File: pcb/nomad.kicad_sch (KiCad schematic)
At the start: 36 parts, among them J1 USB_C_Receptacle_USB2.0_16P, J2 Conn_Coaxial, SW1 SW_Push, SW2 SW_Push, SW3 SW_Push, SW4 SW_Push, SW5 SW_Push, SW6 SW_Push, SW7 SW_Push, U1 ESP32-S3-WROOM-1, U2 PCF8574T, U3 BME280, U4 NEO-M8M, U5 CH343G, U7 AMS1117-3.3

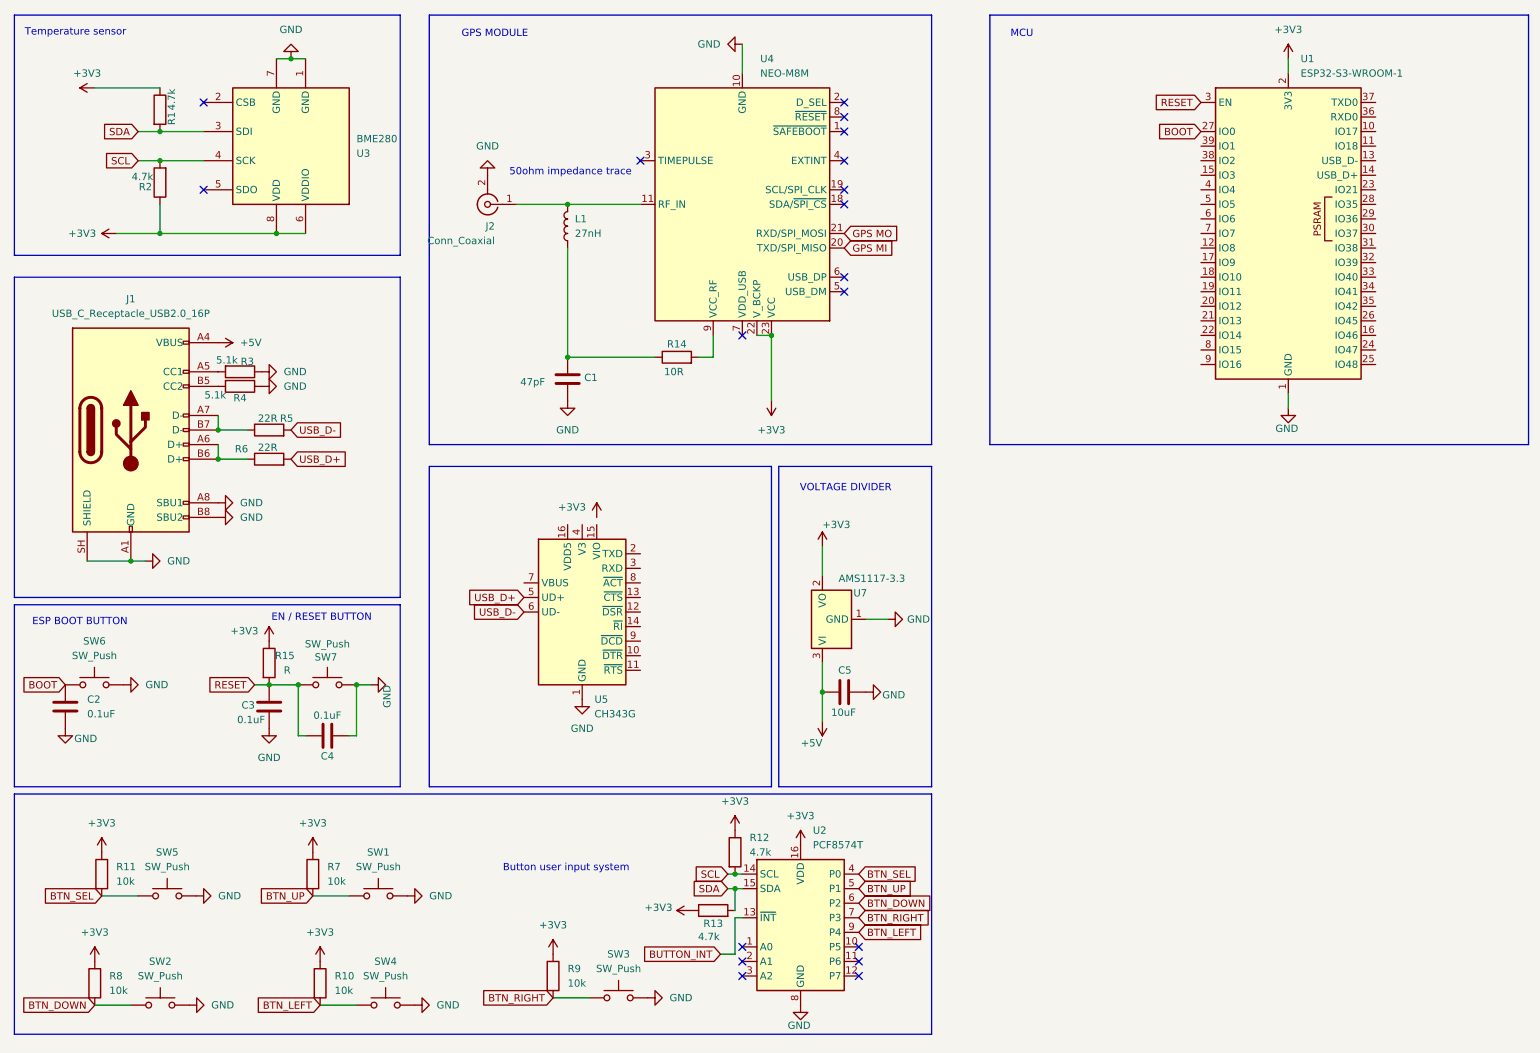
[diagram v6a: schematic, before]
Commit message: Separating modules schematic with system schematic
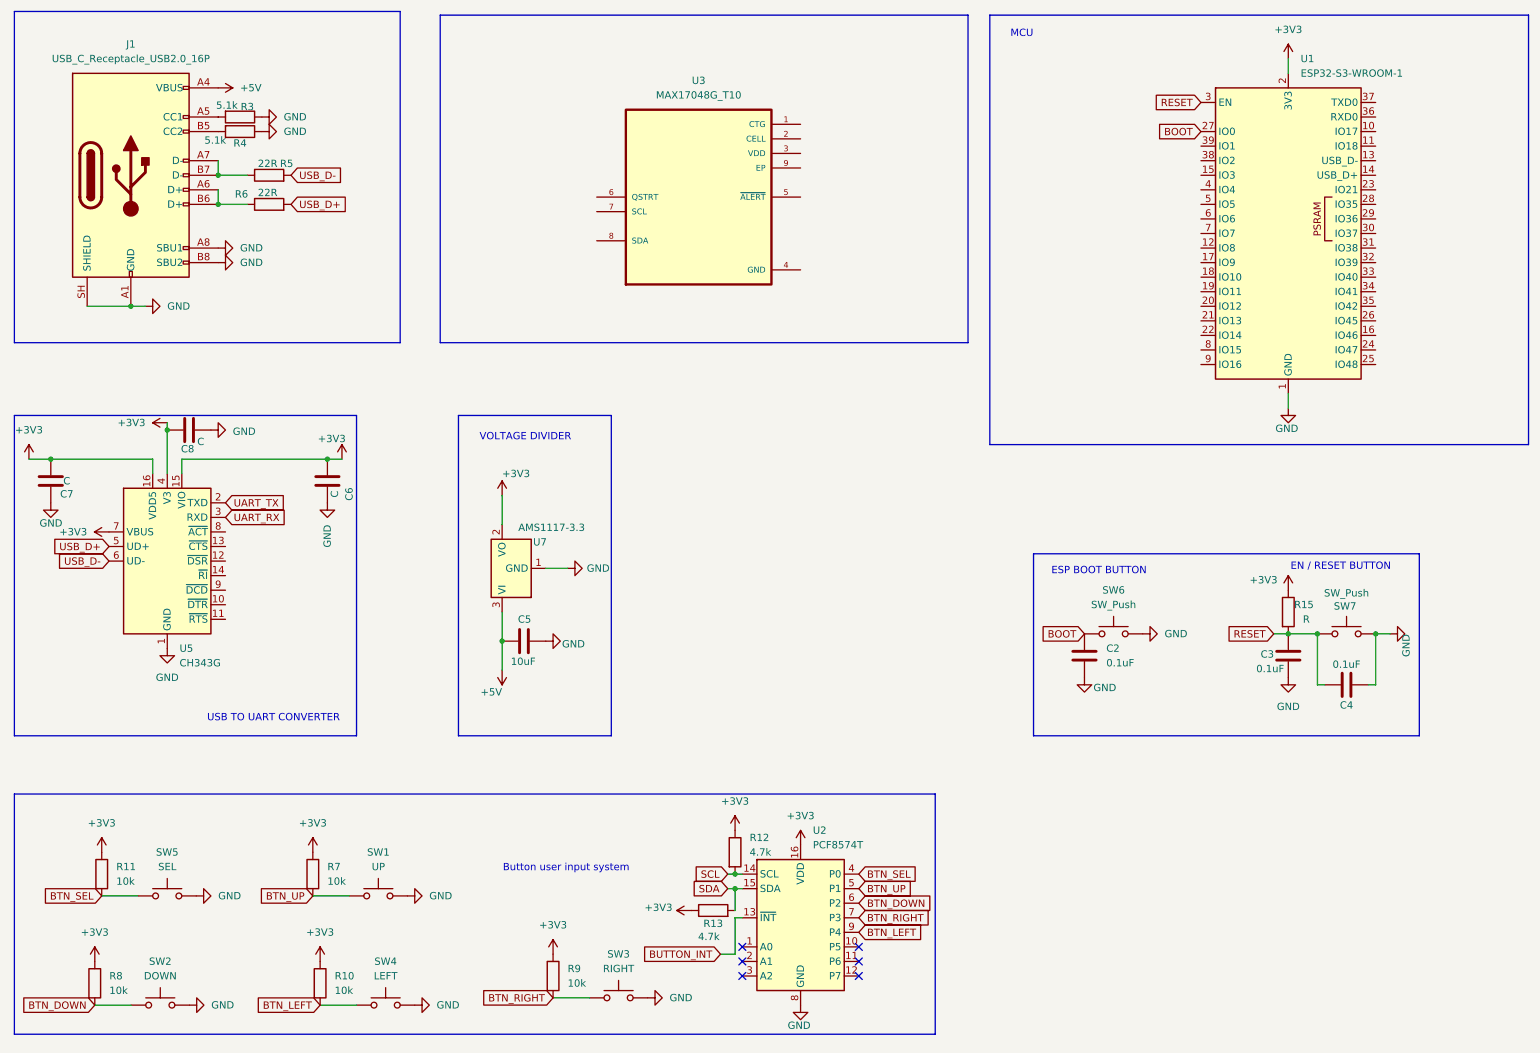
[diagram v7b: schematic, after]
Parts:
- removed C1: 47pF, Capacitor_SMD:C_0805_2012Metric, symbol Device:C
- removed J2: Conn_Coaxial, symbol Connector:Conn_Coaxial
- removed L1: 27nH, symbol Device:L
- removed R1, R2: 4.7k, symbol Device:R
- removed R14: 10R, symbol Device:R
- removed U3: BME280, Package_LGA:Bosch_LGA-8_2.5x2.5mm_P0.65mm_ClockwisePinNumbering, symbol Sensor:BME280
- removed U4: NEO-M8M, RF_GPS:ublox_NEO, symbol RF_GPS:NEO-M8M
- added C6, C7, C8: C, symbol Device:C
- added U3: MAX17048G_T10, MAX17048G_T10:SON50P200X200X80-9N, symbol MAX17048G_T10:MAX17048G_T10
- R10, R11, R12, R13, R15, R3, R4, R5, R6, R7, R8, R9: footprint (none) -> Resistor_SMD:R_0805_2012Metric
- SW1: value SW_Push -> UP; footprint (none) -> Button_Switch_THT:SW_PUSH_6mm
- SW2: value SW_Push -> DOWN; footprint (none) -> Button_Switch_THT:SW_PUSH_6mm
- SW3: value SW_Push -> RIGHT; footprint (none) -> Button_Switch_THT:SW_PUSH_6mm
- SW4: value SW_Push -> LEFT; footprint (none) -> Button_Switch_THT:SW_PUSH_6mm
- SW5: value SW_Push -> SEL; footprint (none) -> Button_Switch_THT:SW_PUSH_6mm
- SW6, SW7: footprint (none) -> Button_Switch_SMD:SW_SPST_SKQG_WithStem
- U1: footprint RF_Module:ESP32-S3-WROOM-1 -> RF_Module:ESP32-S3-WROOM-1U
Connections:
- net +3V3: now also U5.15 (VIO), U5.16 (VDD5), U5.4 (V3), U5.7 (VBUS), C6.1, C7.2, C8.1
- net GND: now also C6.2, C7.1, C8.2
- net UART_TX: now reaches U5.2 (TXD)
- net UART_RX: now reaches U5.3 (RXD)
- no-connect marks 18 -> 6
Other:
- note added: "USB TO UART CONVERTER"
- note removed: "50ohm impedance trace"
- note removed: "GPS MODULE"
- note removed: "Temperature sensor"
- moved on the sheet: C2, C3, C4, C5, J1, R15, R3, R4, R5, R6, SW6, SW7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

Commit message: Updating schematic & pcb & BOM
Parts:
- added C1, C10, C11: C, symbol Device:C
- C5, C6, C7, C8: footprint (none) -> Capacitor_SMD:C_0805_2012Metric
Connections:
- net +3V3: now also C1.1, C10.1, C11.1
- net GND: now also U3.4 (GND), C1.2, C10.2, C11.2
- net SCL: now also U3.7 (SCL)
- net SDA: now also U3.8 (SDA)
- net UART_RX: now also U1.37 (TXD0)
- net UART_TX: now also U1.36 (RXD0)
- no-connect marks 6 -> 11
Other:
- moved on the sheet: U1, U3
